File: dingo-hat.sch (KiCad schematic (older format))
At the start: 46 parts, among them J1 6-13V, J14 NEOPIXEL, J15 MPU-9250, J2 Raspberry_Pi_2_3, J24 3mm_Mount, J25 3mm_Mount, J26 3mm_Mount, J27 3mm_Mount, J3 ULTRA_0, J4 ULTRA_1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

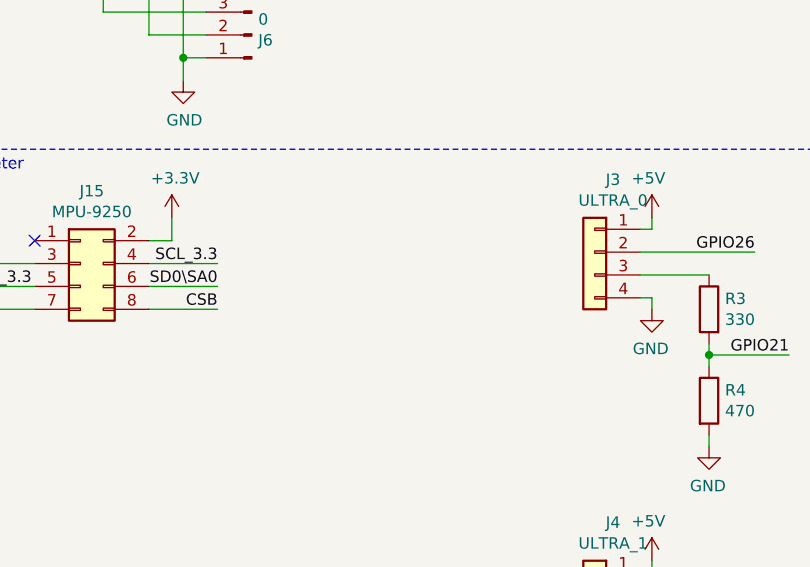
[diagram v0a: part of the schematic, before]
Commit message: Added i2c header
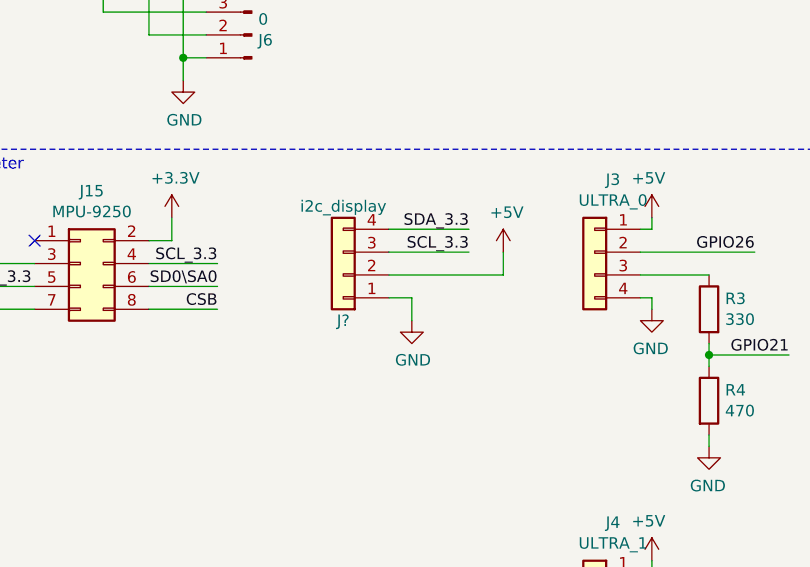
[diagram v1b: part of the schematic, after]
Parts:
- added J?: i2c_display, Connector_PinSocket_2.54mm:PinSocket_1x04_P2.54mm_Vertical, symbol Connector_Generic:Conn_01x04
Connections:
- net +5V: now also J?.2 (Pin_2)
- net GND: now also J?.1 (Pin_1)
- net SCL_3.3: now also J?.3 (Pin_3)
- net SDA_3.3: now also J?.4 (Pin_4)
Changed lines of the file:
@@
 Wire Wire Line
 	8800 3650 8800 3550
+$Comp
+L Connector_Generic:Conn_01x04 J?
+U 1 1 5DB725E6
+P 6200 2950
+F 0 "J?" H 6200 3150 50  0000 C CNN
+F 1 "i2c_display" H 6200 2650 50  0000 C CNN
+F 2 "Connector_PinSocket_2.54mm:PinSocket_1x04_P2.54mm_Vertical" H 6200 2950 50  0001 C CNN
+F 3 "~" H 6200 2950 50  0001 C CNN
+F 4 "https://tronixlabs.com.au/sensors/distance/ultrasonic/ultrasonic-distance-sensor-module-hc-sr04-2-450-cm-australia/" H 6200 2950 50  0001 C CNN "Link"
+	1    6200 2950
+	-1   0    0    1
+$EndComp
+$Comp
+L power:GND #PWR?
+U 1 1 5DB85148
+P 6500 3150
+F 0 "#PWR?" H 6500 2900 50  0001 C CNN
+F 1 "GND" H 6505 2977 50  0000 C CNN
+F 2 "" H 6500 3150 50  0001 C CNN
+F 3 "" H 6500 3150 50  0001 C CNN
+	1    6500 3150
+	1    0    0    -1
+$EndComp
+Text Label 6750 2750 2    50   ~ 0
+SDA_3.3
+Text Label 6750 2850 2    50   ~ 0
+SCL_3.3
+$Comp
+L power:+5V #PWR?
+U 1 1 5DB85AD4
+P 6900 2850
+F 0 "#PWR?" H 6900 2700 50  0001 C CNN
+F 1 "+5V" H 6915 3023 50  0000 C CNN
+F 2 "" H 6900 2850 50  0001 C CNN
+F 3 "" H 6900 2850 50  0001 C CNN
+	1    6900 2850
+	1    0    0    -1
+$EndComp
+Wire Wire Line
+	6900 2850 6900 2950
+Wire Wire Line
+	6900 2950 6400 2950
+Wire Wire Line
+	6400 3050 6500 3050
+Wire Wire Line
+	6500 3050 6500 3150
+Wire Wire Line
+	6750 2850 6400 2850
+Wire Wire Line
+	6750 2750 6400 2750
 $EndSCHEMATC

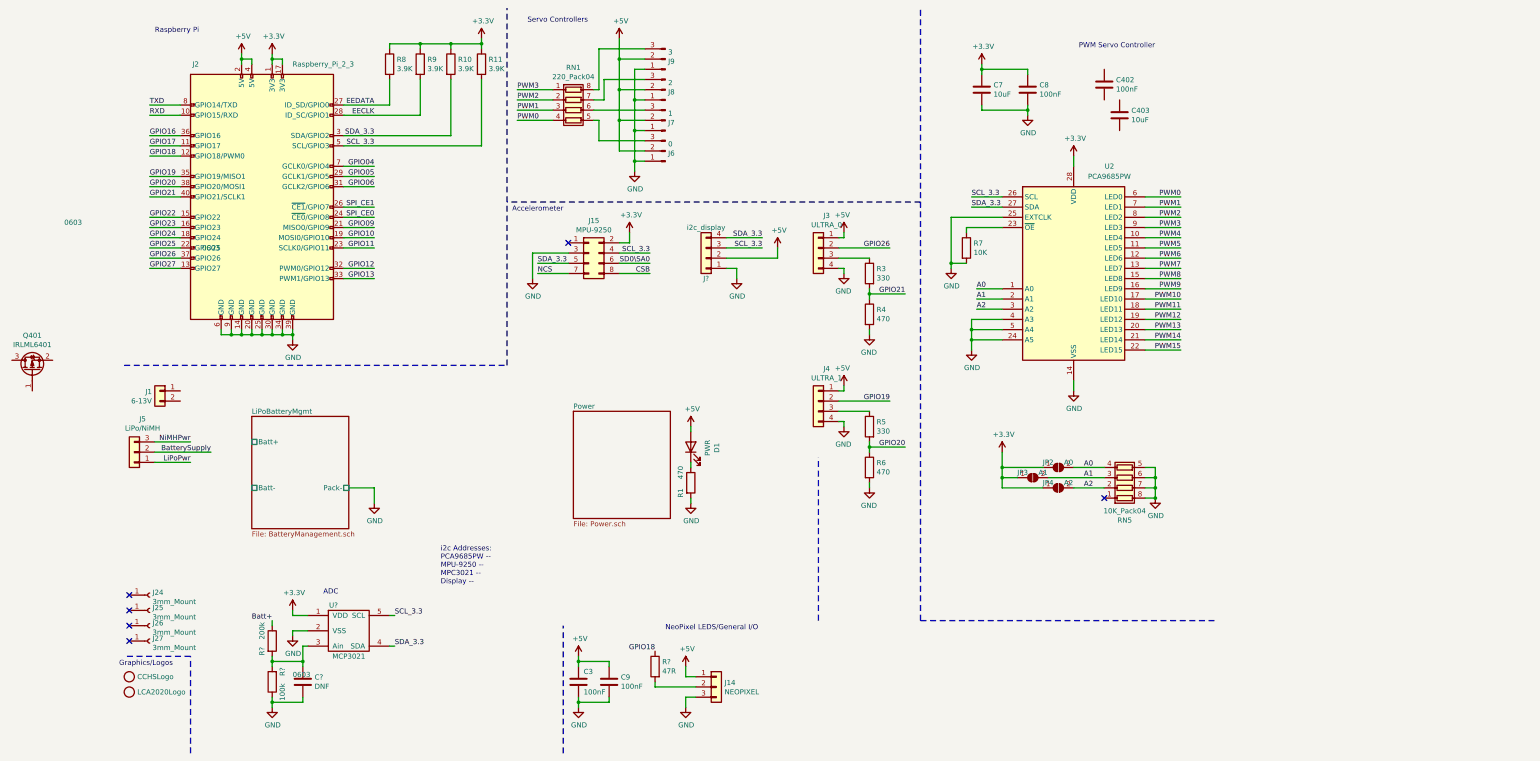
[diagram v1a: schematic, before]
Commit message: Placeholders for some connectors.
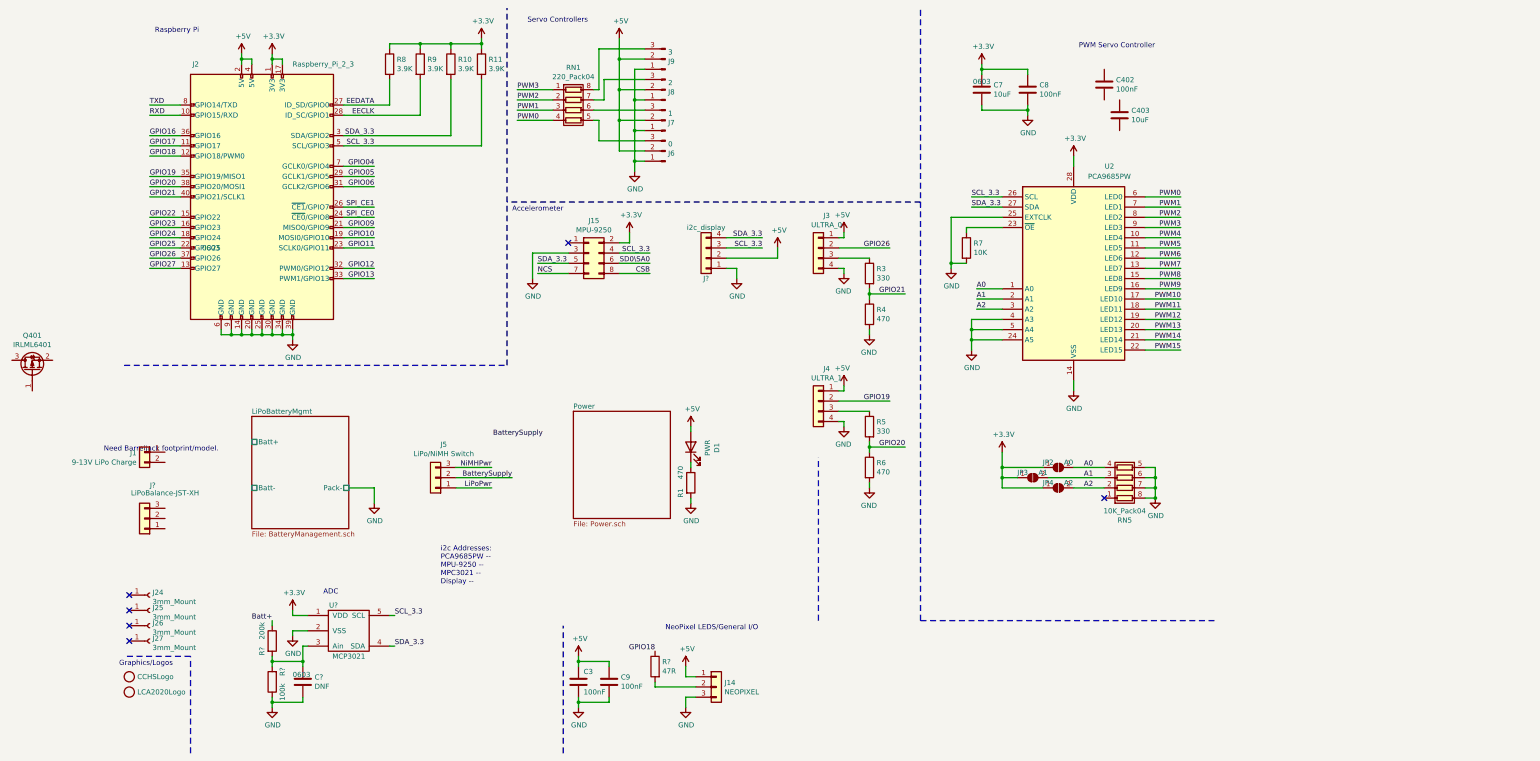
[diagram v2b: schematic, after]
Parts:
- added J?: LiPoBalance-JST-XH, Connector_PinHeader_2.54mm:PinHeader_1x03_P2.54mm_Vertical, symbol Connector_Generic:Conn_01x03
- J1: value 6-13V -> 9-13V LiPo Charge; footprint Connector_Phoenix_MC:PhoenixContact_MC_1,5_2-G-3.5_1x02_P3.50mm_Horizontal -> (none)
- J5: value LiPo/NiMH -> LiPo/NiMH Switch
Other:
- note added: "Need BarrelJack footprint/model."
- moved on the sheet: J1, J5
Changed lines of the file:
@@
 EESchema Schematic File Version 4
 LIBS:dingo-hat-cache
-EELAYER 29 0
+EELAYER 30 0
 EELAYER END
 $Descr A4 11693 8268
@@
 F 2 "Capacitor_SMD:C_0603_1608Metric_Pad1.05x0.95mm_HandSolder" H 8938 1150 50  0001 C CNN
 F 3 "~" H 8900 1300 50  0001 C CNN
-F 4 "0603" H 0   0   50  0000 C CNN "Package"
+F 4 "0603" H 8900 1350 50  0000 C BNN "Package"
 	1    8900 1300
 	1    0    0    -1
@@
 L Connector_Generic:Conn_01x02 J1
 U 1 1 5C20A2ED
-P 850 4250
-F 0 "J1" H 929 4242 50  0000 L CNN
-F 1 "6-13V" H 929 4151 50  0000 L CNN
-F 2 "Connector_Phoenix_MC:PhoenixContact_MC_1,5_2-G-3.5_1x02_P3.50mm_Horizontal" H 850 4250 50  0001 C CNN
-F 3 "~" H 850 4250 50  0001 C CNN
-	1    850  4250
+P 700 4850
+F 0 "J1" H 779 4842 50  0000 L CNN
+F 1 "9-13V LiPo Charge" H 779 4751 50  0000 L CNN
+F 2 "" H 700 4850 50  0001 C CNN
+F 3 "~" H 700 4850 50  0001 C CNN
+	1    700  4850
 	-1   0    0    -1
 $EndComp
@@
 Wire Notes Line
 	7300 6500 7300 4900
-Text Label 1150 4750 2    50   ~ 0
+Text Label 4100 5000 2    50   ~ 0
 NiMHPwr
-Text Label 1150 4950 2    50   ~ 0
+Text Label 4100 5200 2    50   ~ 0
 LiPoPwr
 $Comp
 L Connector_Generic:Conn_01x03 J5
 U 1 1 5C1E72E1
-P 600 4850
-F 0 "J5" H 520 4525 50  0000 C CNN
-F 1 "LiPo/NiMH" H 520 4616 50  0000 C CNN
-F 2 "Connector_PinHeader_2.54mm:PinHeader_1x03_P2.54mm_Vertical" H 600 4850 50  0001 C CNN
-F 3 "~" H 600 4850 50  0001 C CNN
-	1    600  4850
+P 3550 5100
+F 0 "J5" H 3470 4775 50  0000 C CNN
+F 1 "LiPo/NiMH Switch" H 3470 4866 50  0000 C CNN
+F 2 "Connector_PinHeader_2.54mm:PinHeader_1x03_P2.54mm_Vertical" H 3550 5100 50  0001 C CNN
+F 3 "~" H 3550 5100 50  0001 C CNN
+	1    3550 5100
 	-1   0    0    1
 $EndComp
-Text Label 1350 4850 2    50   ~ 0
+Text Label 4300 5100 2    50   ~ 0
 BatterySupply
 $Sheet
@@
 $EndSheet
 Wire Wire Line
-	800  4750 1150 4750
-Wire Wire Line
-	800  4950 1150 4950
-Wire Wire Line
-	800  4850 1350 4850
+	3750 5000 4100 5000
+Wire Wire Line
+	3750 5200 4100 5200
+Wire Wire Line
+	3750 5100 4300 5100
 $Comp
 L power:GND #PWR0401
@@
 Wire Wire Line
 	6750 2750 6400 2750
+$Comp
+L Connector_Generic:Conn_01x03 J?
+U 1 1 5DBAD292
+P 700 5500
+F 0 "J?" H 620 5175 50  0000 C CNN
+F 1 "LiPoBalance-JST-XH" H 500 5250 50  0000 C CNN
+F 2 "Connector_PinHeader_2.54mm:PinHeader_1x03_P2.54mm_Vertical" H 700 5500 50  0001 C CNN
+F 3 "~" H 700 5500 50  0001 C CNN
+	1    700  5500
+	-1   0    0    1
+$EndComp
+Text Label 4600 4700 2    50   ~ 0
+BatterySupply
+Text Notes 300  4850 0    50   ~ 0
+Need BarrelJack footprint/model.
 $EndSCHEMATC

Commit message: Cleaning up some nets, adding input caps on power.
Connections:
- net Batt+ is gone; now on net BatterySupply: R?.1
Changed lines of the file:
@@
 F0 "Power" 50
 F1 "Power.sch" 50
+F2 "Supply" I L 4900 4750 50
 $EndSheet
 Wire Notes Line
@@
 Wire Wire Line
 	1950 6900 1950 6950
-Text Label 1950 6500 2    50   ~ 0
-Batt+
 Wire Wire Line
 	1950 6500 1950 6550
@@
 	-1   0    0    1
 $EndComp
-Text Label 4600 4700 2    50   ~ 0
+Text Label 1950 6500 2    50   ~ 0
 BatterySupply
 Text Notes 300  4850 0    50   ~ 0
 Need BarrelJack footprint/model.
+Text Label 4750 4750 2    50   ~ 0
+BatterySupply
+Wire Wire Line
+	4900 4750 4750 4750
 $EndSCHEMATC

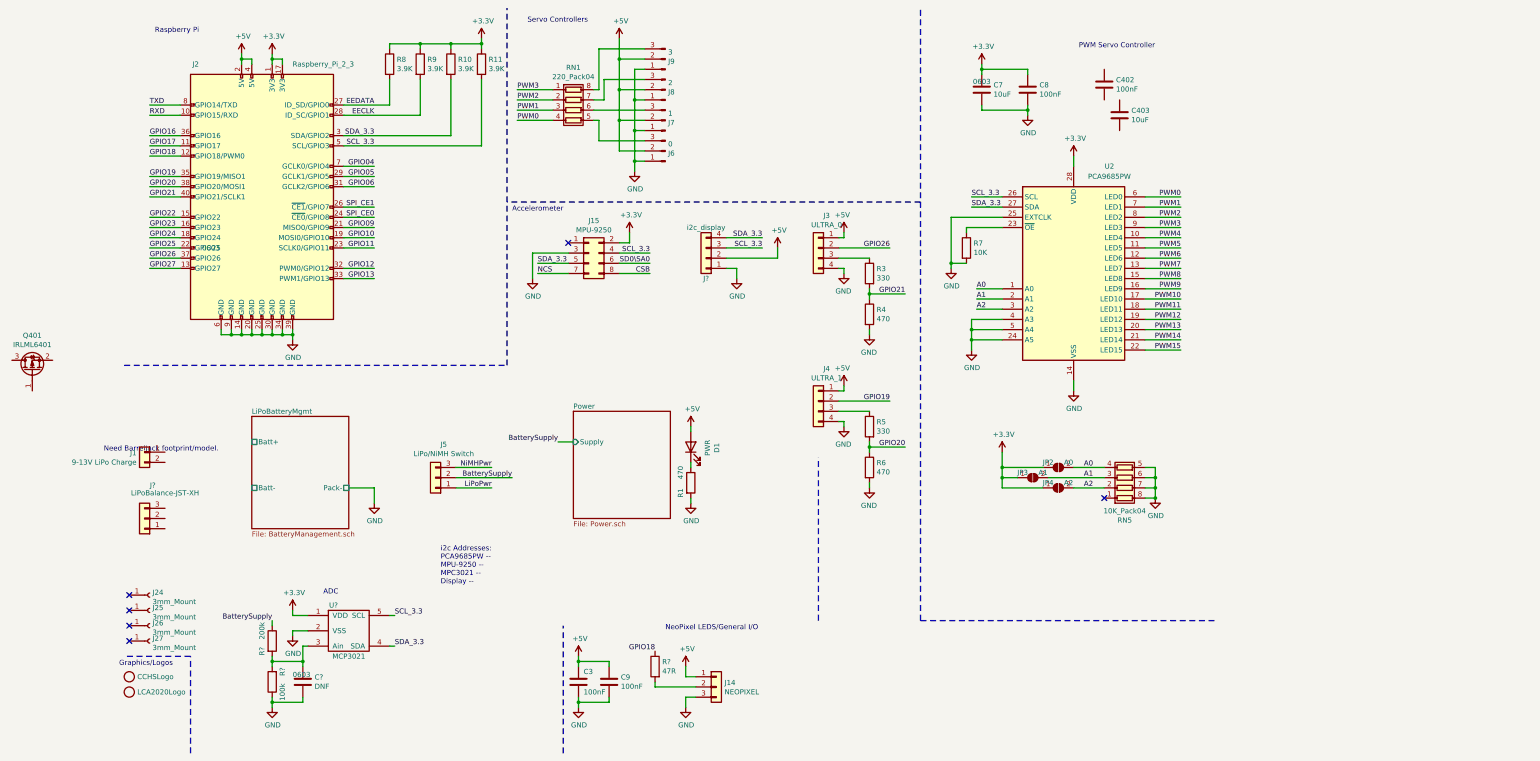
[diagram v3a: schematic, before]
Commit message: Power protection.
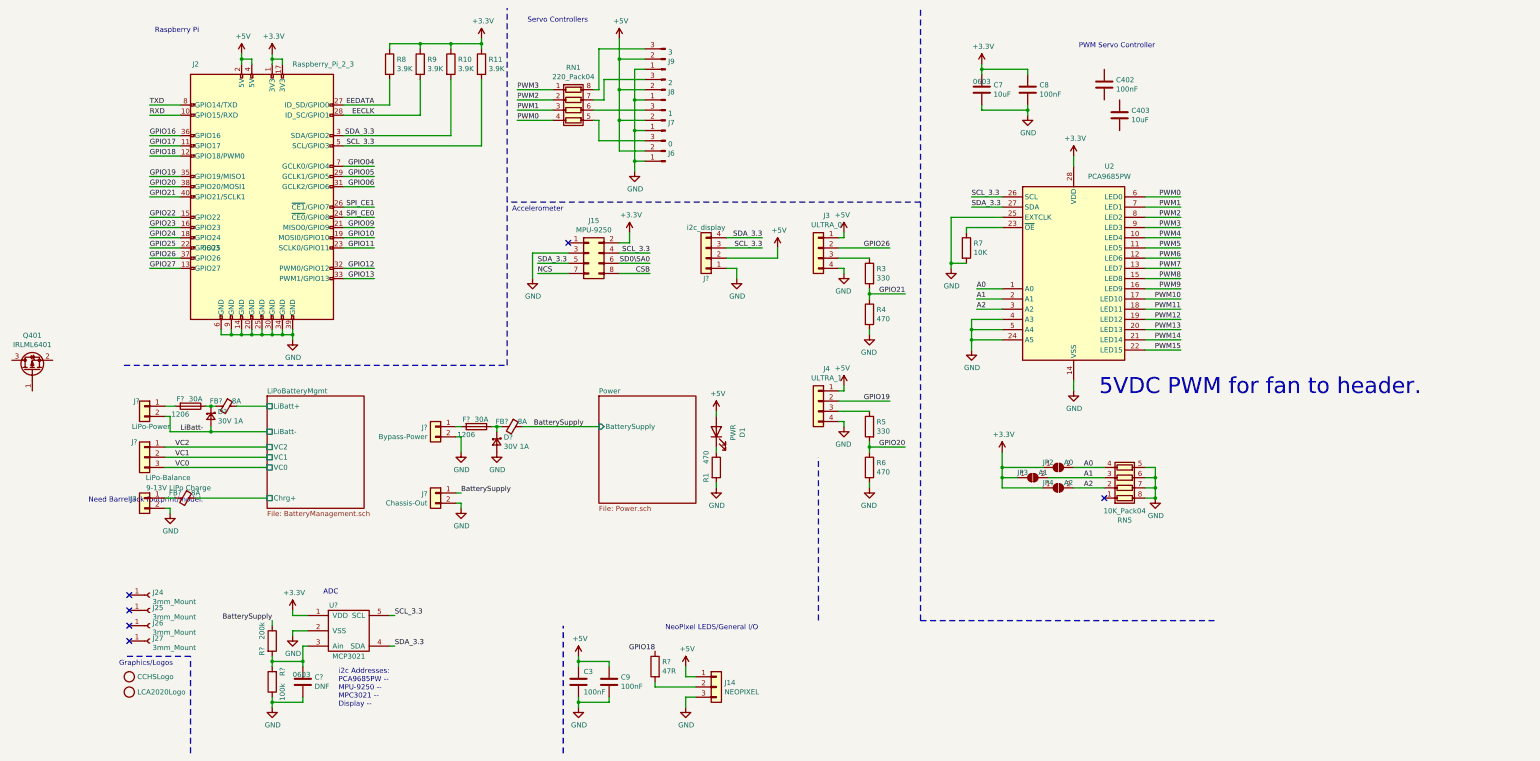
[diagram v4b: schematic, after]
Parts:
- removed J5: LiPo/NiMH Switch, Connector_PinHeader_2.54mm:PinHeader_1x03_P2.54mm_Vertical, symbol Connector_Generic:Conn_01x03
- added D? (x2): 30V 1A, Diodes_SMD:D_SOD-123F, symbol Device:D_Schottky_Small
- added F? (x2): Fuse, Resistors_SMD:R_1206, symbol Device:Fuse
- added FB? (x3): Ferrite_Bead_Small, Resistors_SMD:R_0603, symbol Device:Ferrite_Bead_Small
- added J?: LiPo-Power, libs:SolderWirePad_2x_5.08mm_14-18AWG-2mmDrill, symbol Connector_Generic:Conn_01x02
- added J?: Bypass-Power, libs:SolderWirePad_2x_5.08mm_14-18AWG-2mmDrill, symbol Connector_Generic:Conn_01x02
- added J?: Chassis-Out, libs:SolderWirePad_2x_5.08mm_14-18AWG-2mmDrill, symbol Connector_Generic:Conn_01x02
- J?: value LiPoBalance-JST-XH -> LiPo-Balance; footprint Connector_PinHeader_2.54mm:PinHeader_1x03_P2.54mm_Vertical -> Connectors_JST:JST_XH_S03B-XH-A_03x2.50mm_Angled
- renumbered J1 to J?
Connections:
- net BatterySupply: now also FB?.1, J?.1 (Pin_1)
- net GND: now also J?.2 (Pin_2), D?.2 (A), J?.2 (Pin_2), J?.2 (Pin_2)
- net at J?.1 (Pin_1): now also FB?.2
- net VC2: now reaches J?.1 (Pin_1)
- net VC1: now reaches J?.2 (Pin_2)
- net VC0: now reaches J?.3 (Pin_3)
- new net: D?.1 (K), F?.1, FB?.2 (x2)
- new net: F?.2, J?.1 (Pin_1) (x2)
- new net LiBatt-: D?.2 (A), J?.2 (Pin_2)
- new net LiPoBatteryMgmt/Chrg+: FB?.1
- new net LiPoBatteryMgmt/LiBatt+: FB?.1
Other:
- note added: "5VDC PWM for fan to header."
- moved on the sheet: D1, J?, R1

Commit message: Filling in some footprints, cleaning up schematic.
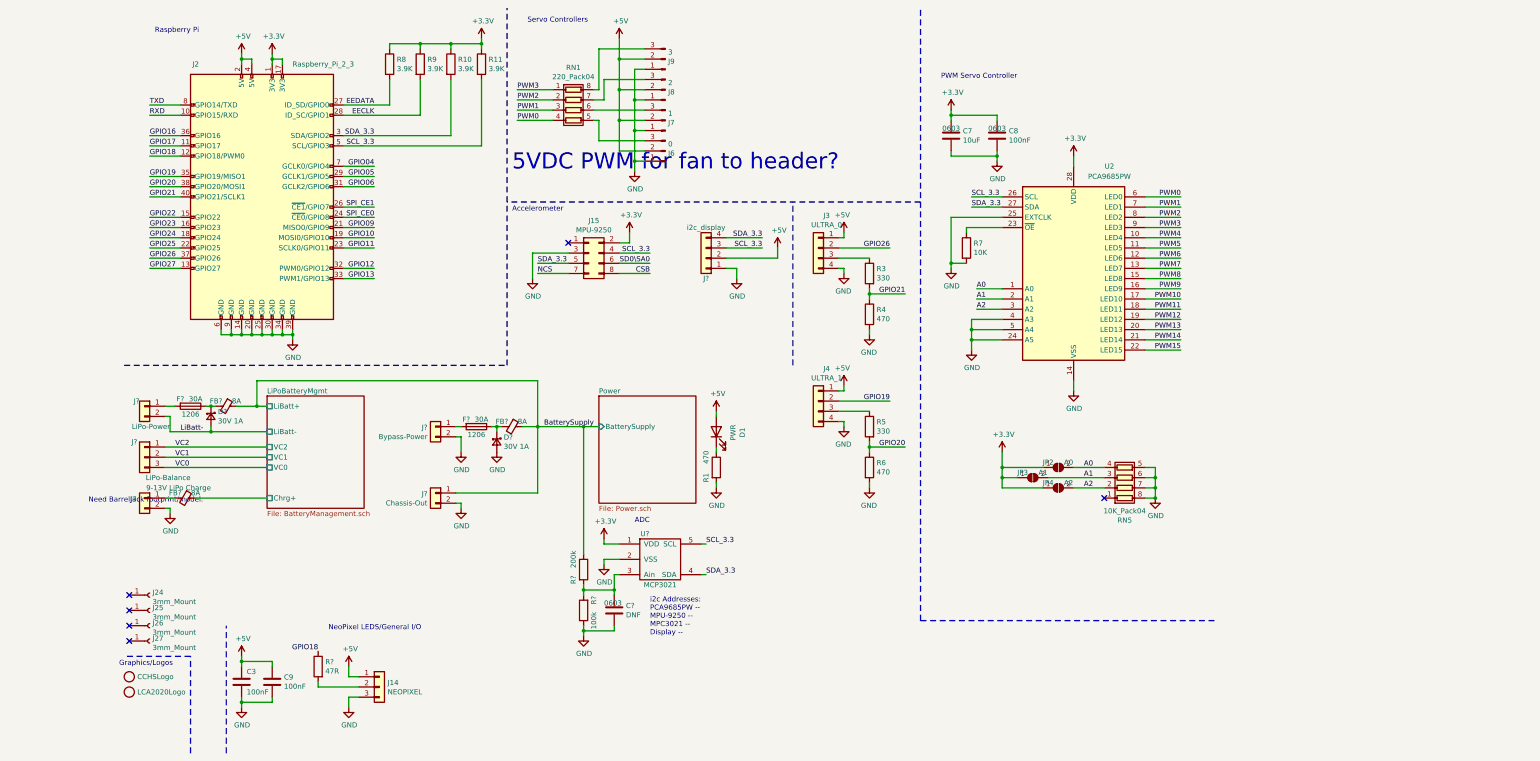
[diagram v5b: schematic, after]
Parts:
- removed C402: 100nF, Capacitor_SMD:C_0603_1608Metric_Pad1.05x0.95mm_HandSolder, symbol Device:C
- removed C403: 10uF, Capacitor_SMD:C_0603_1608Metric_Pad1.05x0.95mm_HandSolder, symbol Device:C
- removed Q401: IRLML6401, Package_TO_SOT_SMD:SOT-23_Handsoldering, symbol Transistor_FET:IRLML6402
- G1: footprint (none) -> libs:logo.cchs
- U?: Description (none) -> IC ADC 10BIT SAR SOT23-5; Link (none) -> https://www.digikey.com.au/product-detail/en/microchip-tech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; Mfg Part # (none) -> MCP3021A5T-E/OT; Package (none) -> SOT-23-5; Supplier 1 (none) -> Digi-Key; Supplier Part Number 1 (none) -> MCP3021A5T-E/OTCT-ND; Unit Cost A$ (none) -> 1.64000
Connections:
- net LiPoBatteryMgmt/LiBatt+ is gone; now on net BatterySupply: FB?.1
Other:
- note added: "5VDC PWM for fan to header?"
- note removed: "5VDC PWM for fan to header."
- moved on the sheet: C3, C7, C8, C9, C?, J14, R?, U?
